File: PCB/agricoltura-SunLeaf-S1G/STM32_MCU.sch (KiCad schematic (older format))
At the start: 34 parts

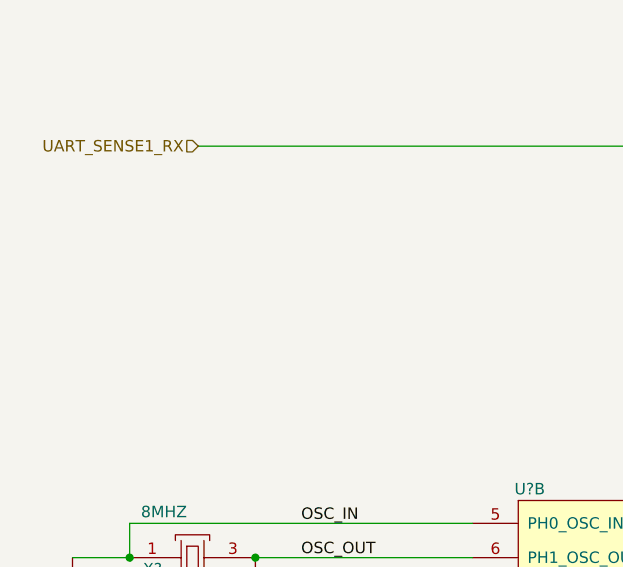
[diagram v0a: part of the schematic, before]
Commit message: Power Supply and Datasheets
Added datasheets for parts in use, designed power supply circuit
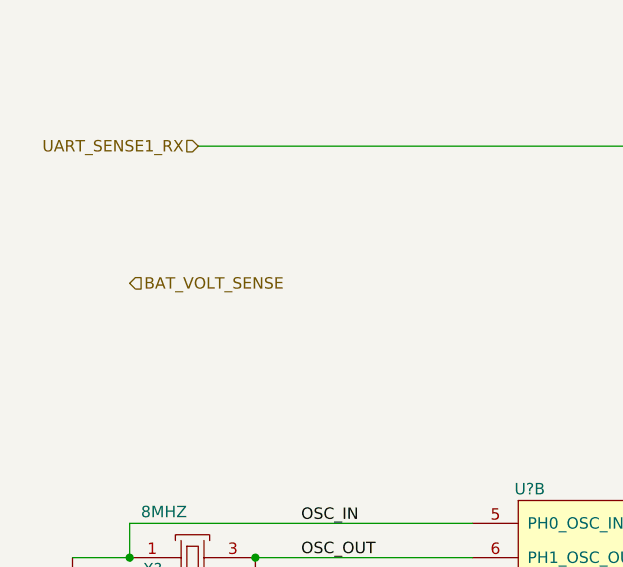
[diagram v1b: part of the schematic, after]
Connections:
- net labels added: BAT_VOLT_SENSE
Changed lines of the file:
@@
 Wire Wire Line
 	9200 2850 8100 2850
+Text HLabel 900  4350 2    50   Input ~ 0
+BAT_VOLT_SENSE
 $EndSCHEMATC

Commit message: Schematic Complete
Schematic completed and PCB started
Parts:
- added D1: LW_Q38G_Q1OO_3K6L_1, AVR-KiCAD-Lib-Diodes:LED0603, symbol AVR-KiCAD-Lib-Diodes:LW_Q38G_Q1OO_3K6L_1
- added L2: MI0603K300R-10, AVR-KiCAD-Lib-Inductors:MI0603K300R-10, symbol AVR-KiCAD-Lib-Inductors:MI0603K300R-10
- added R1: RC0402FR-071KL, AVR-KiCAD-Lib-Resistors:R0402, symbol AVR-KiCAD-Lib-Resistors:RC0402FR-071KL
- added R10: RC0402FR-0710KL, AVR-KiCAD-Lib-Resistors:R0402, symbol AVR-KiCAD-Lib-Resistors:RC0402FR-0710KL
- added R11, R12: RC0402FR-0722RL, AVR-KiCAD-Lib-Resistors:R0402, symbol AVR-KiCAD-Lib-Resistors:RC0402FR-0722RL
- added R14, R15, R18, R2, R3: RC0402FR-0733RL, AVR-KiCAD-Lib-Resistors:R0402, symbol AVR-KiCAD-Lib-Resistors:RC0402FR-0733RL
- gave numbers to parts that had none: 33
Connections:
- net labels added: BAT_VOLT_ADC123_IN10, CS_MCU, CS_RF, HEARBEAT_LED, I2C_SCL_MUX, I2C_SDA_MUX, MISO_MCU, MISO_RF, MOSI_MCU, MOSI_RF, RF_SHDN_MCU, SCLK_MCU, SCLK_RF, UART_MUX_E1, UART_MUX_EN, UART_MUX_S0, UART_TX, USB_VBUS_5V
- wire segments 124 -> 138
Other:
- note added: "STM32F446RET6 - ARM Cortex M4 MCU"
- moved on the sheet: C11, C12, C13, C14, L3, R17, R5, R6, R7, R8, R9, T2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

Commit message: PCB Progress
added TVS diodes fo QWIIC connector serial signals. Did more routing overall.
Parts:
- removed SW1: TL3301NF260QG, AVR-KiCAD-Lib-Mech-Switches:TL3301NF260QG, symbol AVR-KiCAD-Lib-Mech-Switches:TL3301NF260QG
- removed T1: BU2032SM-JJ-GTR, AVR-KiCAD-Lib-Battery-Holders:BU2032SM-JJ-GTR, symbol AVR-KiCAD-Lib-Battery-Holders:BU2032SM-JJ-GTR
- added H1, H2, H3, H4, H5, H6: M2_Plated_Hole, AVR-KiCAD-Lib-Holes_Fasteners:M2_HOLE, symbol AVR-KiCAD-Lib-Holes_Fasteners:M2_Plated_Hole
- added L4: BLM15HG601SN1D, AVR-KiCAD-Lib-Inductors:BLM15HG601SN1D, symbol AVR-KiCAD-Lib-Inductors:BLM15HG601SN1D
- added SW1: B3U-1000P, AVR-KiCAD-Lib-Mech-Switches:B3U-1000P, symbol AVR-KiCAD-Lib-Mech-Switches:B3U-1000P
- added T1: BM04B-SRSS-TB(LF)(SN), AVR-KiCAD-Lib-Connectors:CONN_BM04B-SRSS-TB(LF)(SN), symbol AVR-KiCAD-Lib-Connectors:BM04B-SRSS-TB(LF)(SN)
- added T18, T19: PPTC101LFBN-RC, AVR-KiCAD-Lib-Connectors:Female_Header_Straight_1x10_Pitch2.54mm, symbol AVR-KiCAD-Lib-Connectors:PPTC101LFBN-RC
- added T20: BU2032SM-JJ-GTR, AVR-KiCAD-Lib-Battery-Holders:BU2032SM-JJ-GTR, symbol AVR-KiCAD-Lib-Battery-Holders:BU2032SM-JJ-GTR
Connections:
- net labels added: DEBUG_UART_RX, DEBUG_UART_TX, FGND, UART_RX
- wire segments 138 -> 151
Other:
- moved on the sheet: C11, R18

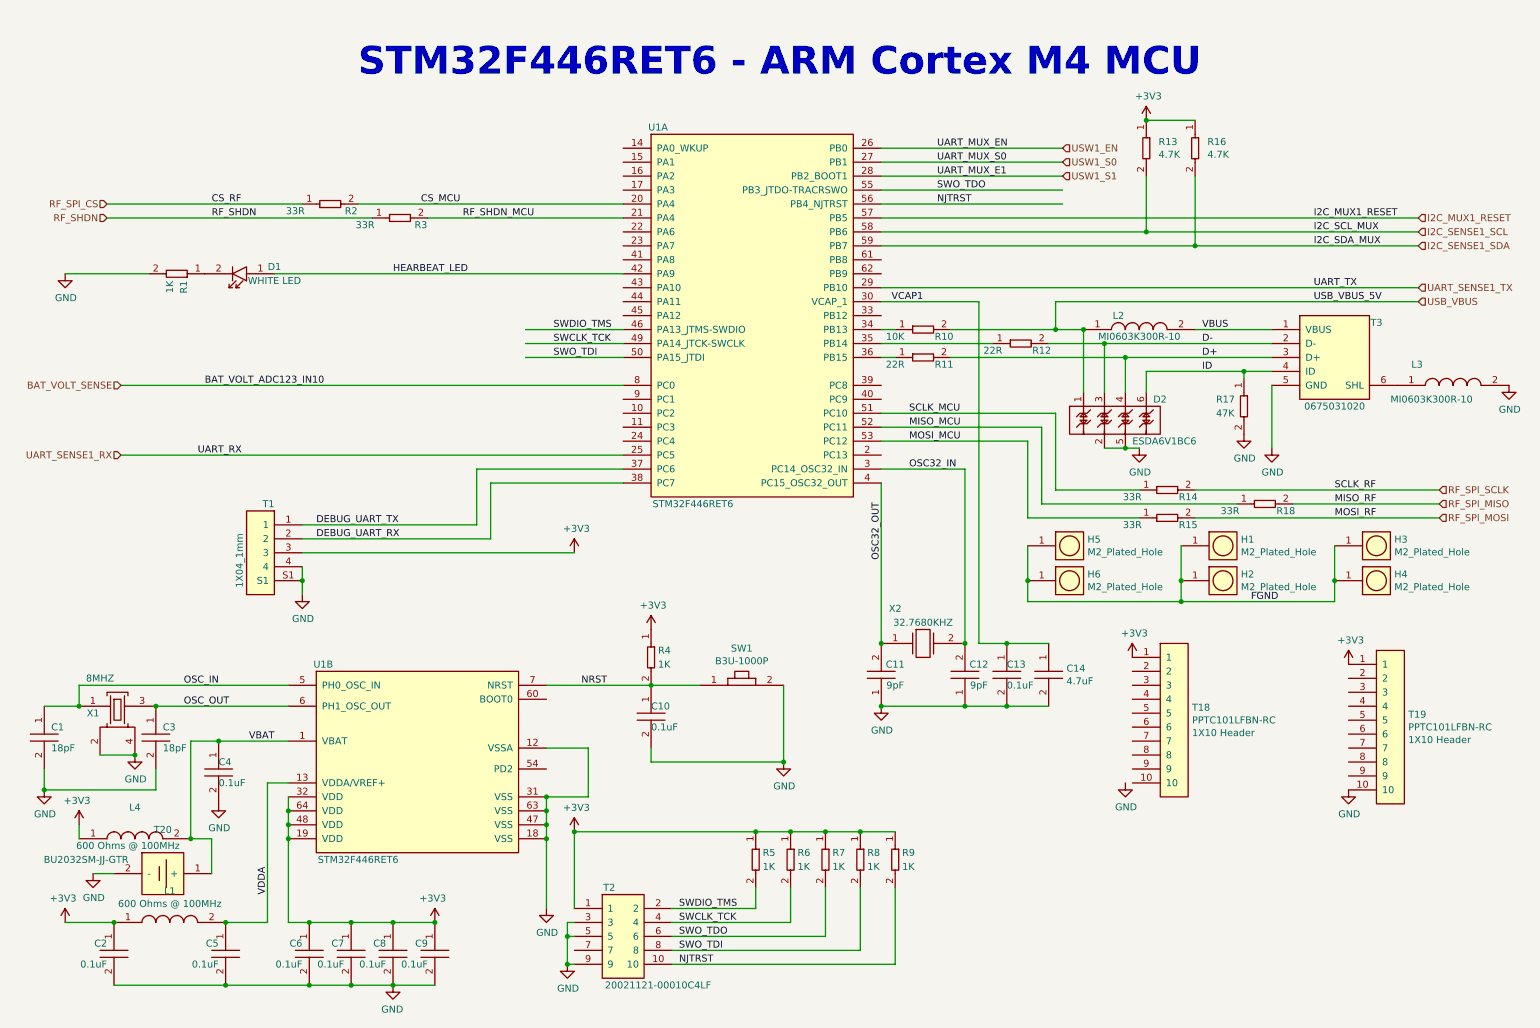
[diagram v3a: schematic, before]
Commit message: Pullups
Added pullup reistors to I2C ports, changed JTAG connector over to Tag connect.
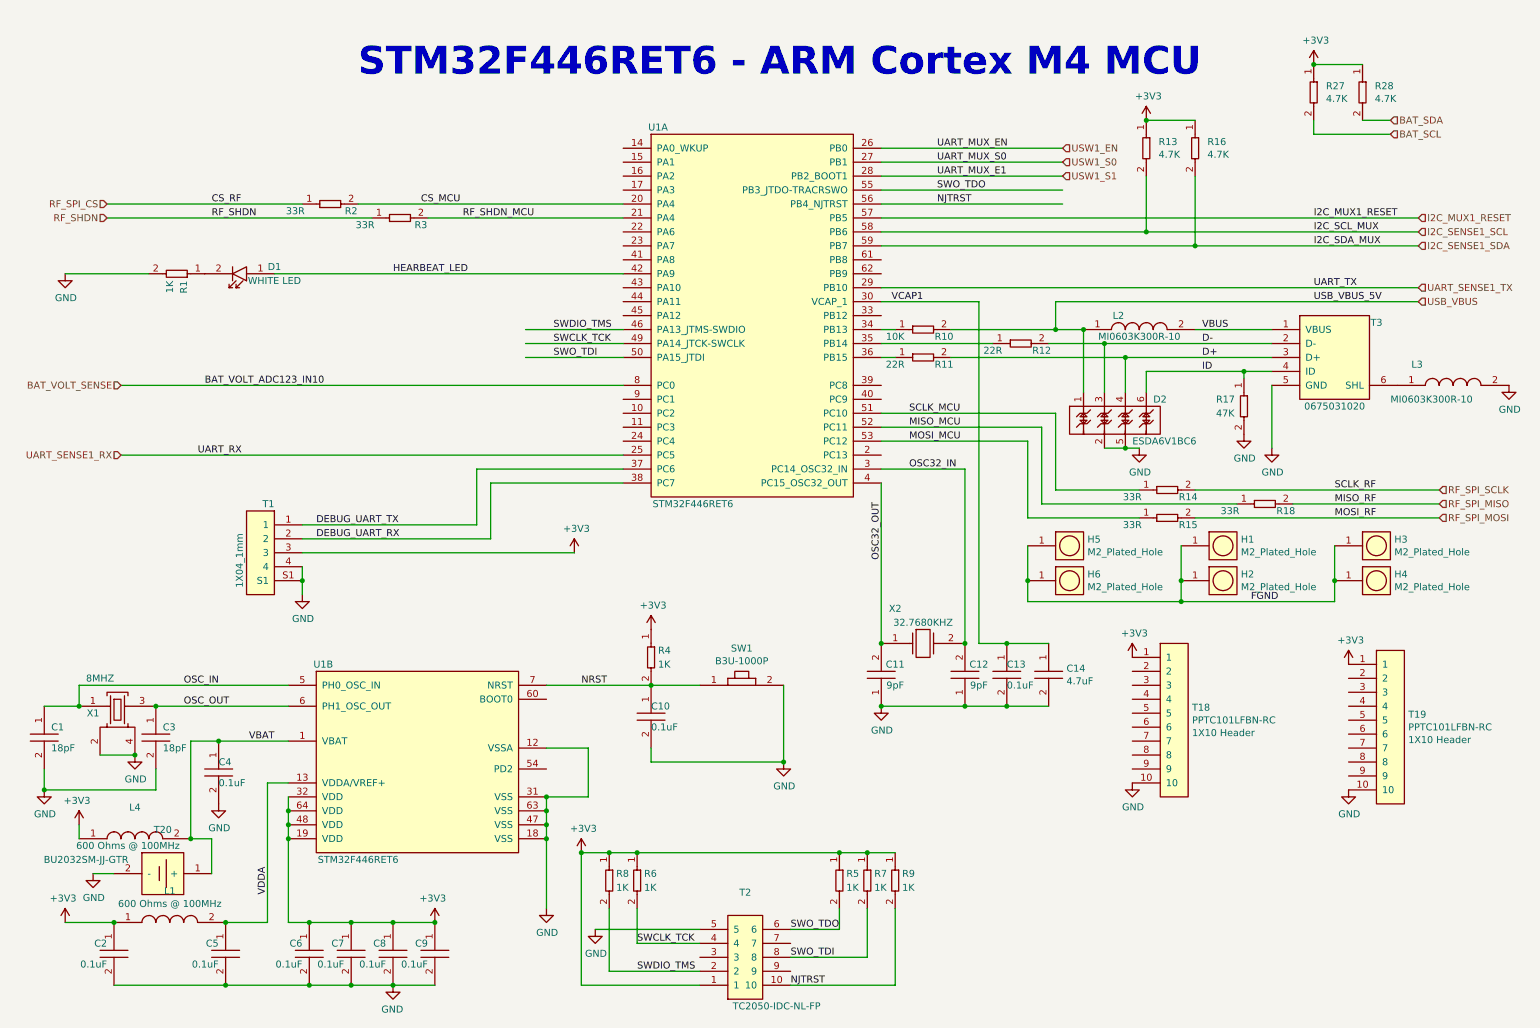
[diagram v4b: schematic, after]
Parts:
- removed T2: 20021121-00010C4LF, AVR-KiCAD-Lib-Connectors:20021121-00010C4LF, symbol AVR-KiCAD-Lib-Connectors:20021121-00010C4LF
- added R27, R28: RC0402FR-074K7L, AVR-KiCAD-Lib-Resistors:R0402, symbol AVR-KiCAD-Lib-Resistors:RC0402FR-074K7L
- added T2: TC2050-IDC-NL-FP, AVR-KiCAD-Lib-Connectors:TC2050-CLIP, symbol AVR-KiCAD-Lib-Connectors:TC2050-IDC-NL-FP
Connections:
- net labels added: BAT_SCL, BAT_SDA
- wire segments 151 -> 152
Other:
- moved on the sheet: R5, R6, R7, R8, R9

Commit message: PCB Progress
PCB routing progress made, USB port replaced with micro b like older sunleaf designs.
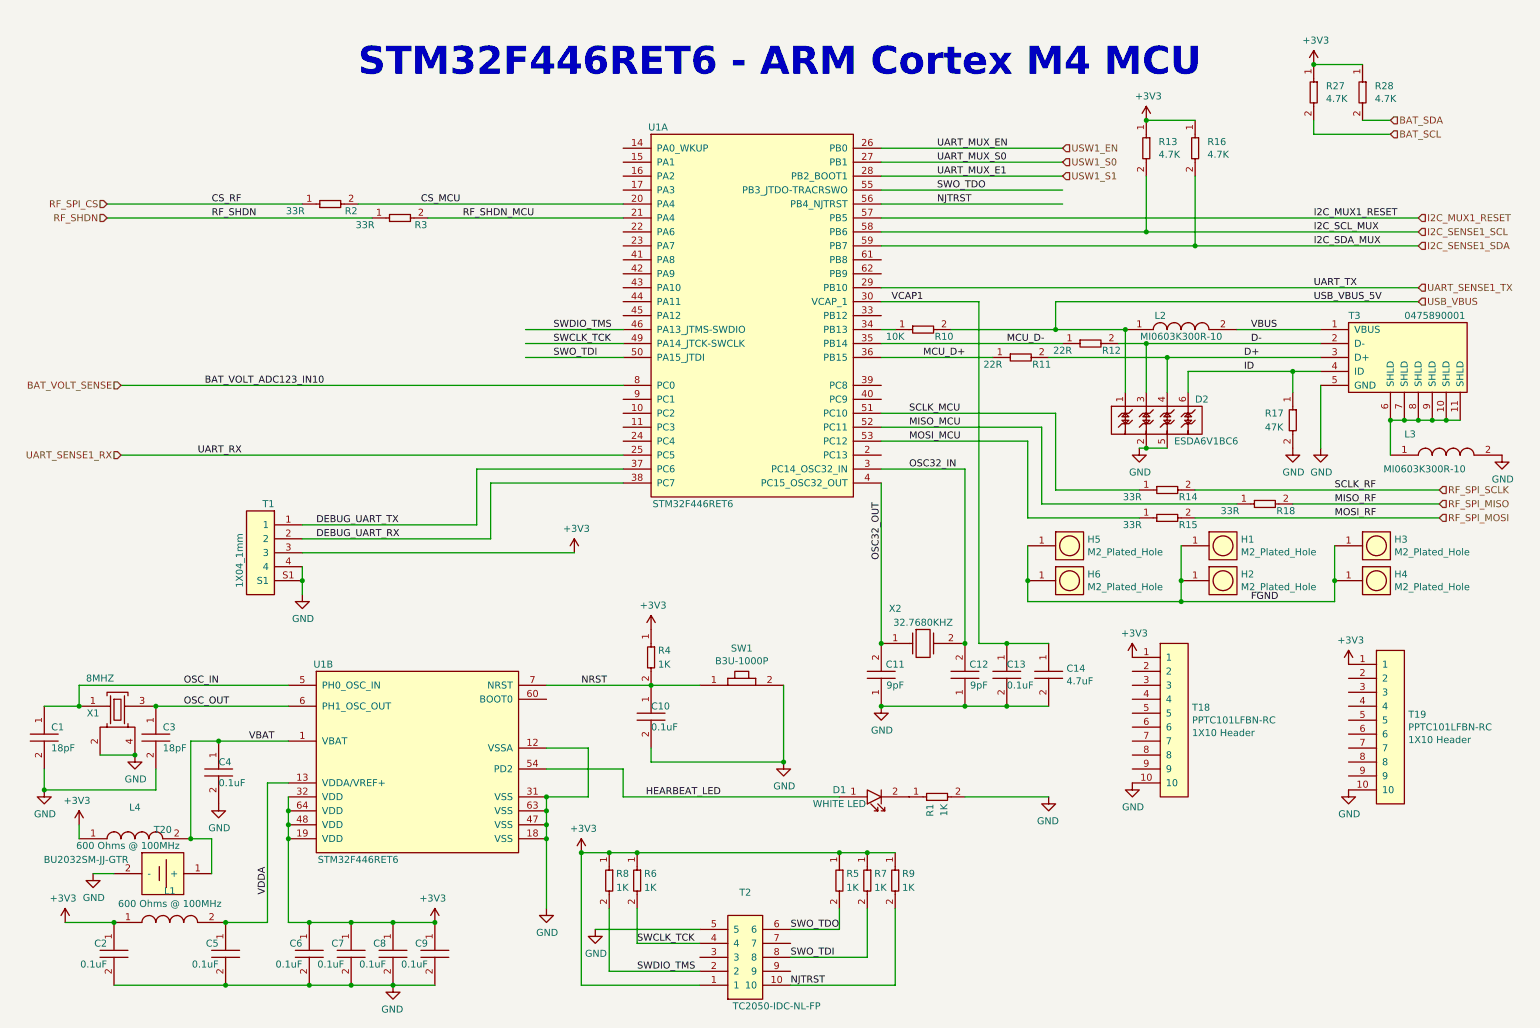
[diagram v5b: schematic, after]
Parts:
- removed T3: 0675031020, AVR-KiCAD-Lib-Connectors:USB_Mini-B, symbol AVR-KiCAD-Lib-Connectors:0675031020
- added T3: 0475890001, AVR-KiCAD-Lib-Connectors:0475890001, symbol AVR-KiCAD-Lib-Connectors:0475890001
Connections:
- net labels added: MCU_D+, MCU_D-
- wire segments 152 -> 160
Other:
- moved on the sheet: D1, D2, L2, L3, R1, R11, R12, R17

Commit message: Routing Complete
Board routing completed, also added EEPROM for storing configuration settings.
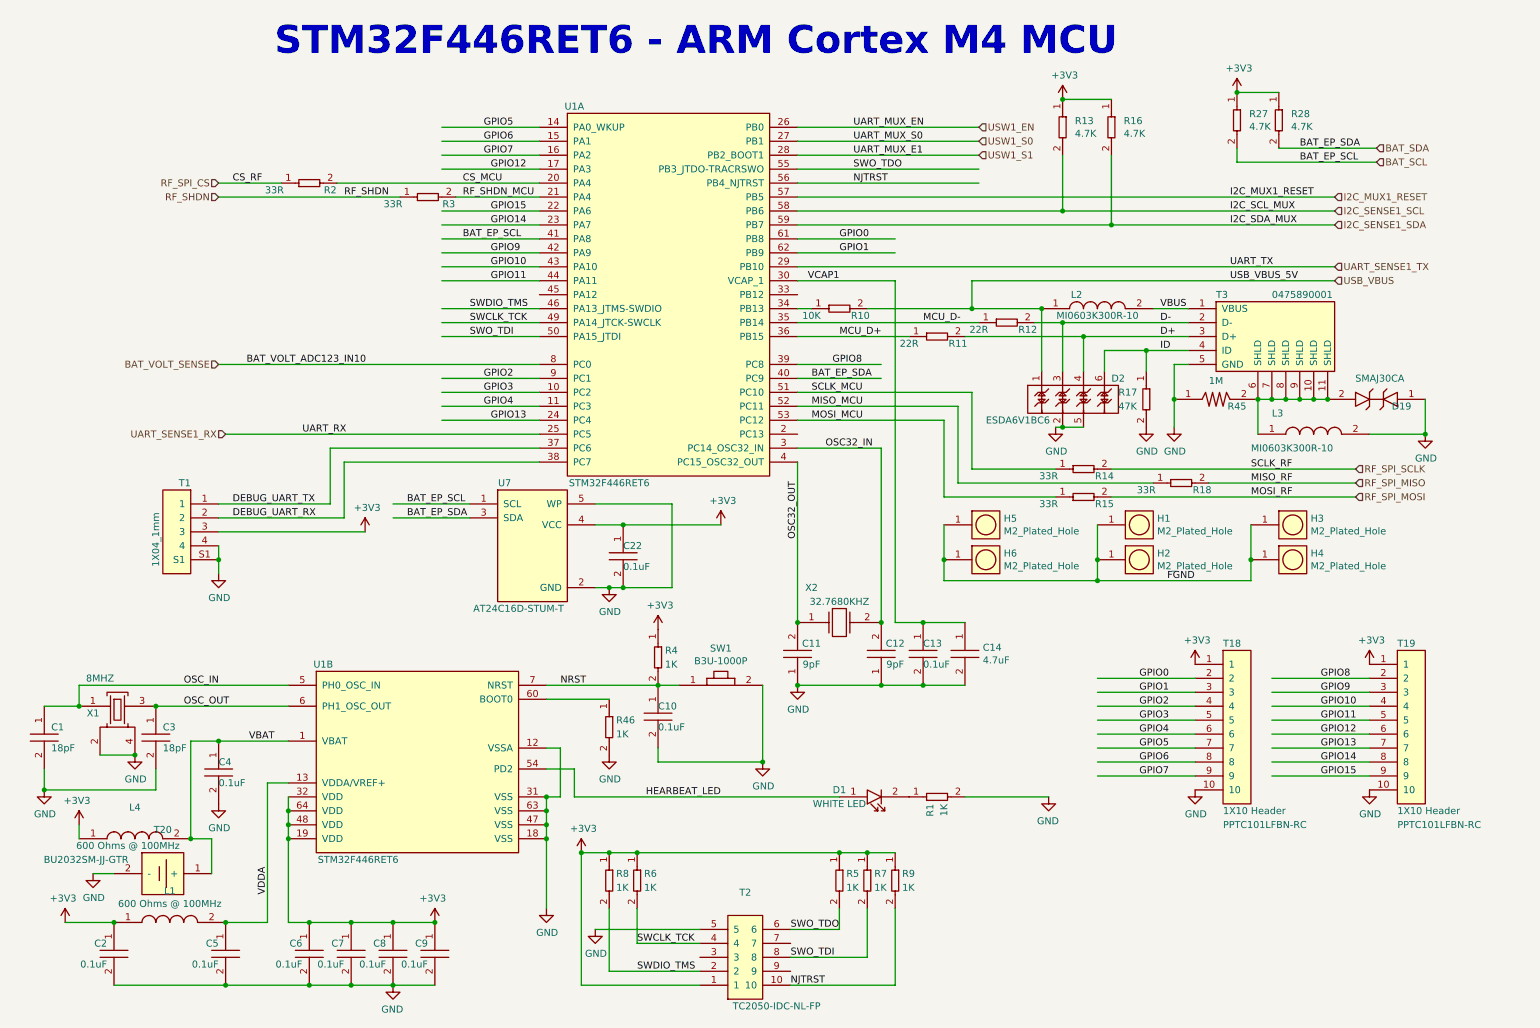
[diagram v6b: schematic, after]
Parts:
- added C22: C0402C104K9PACTU, AVR-KiCAD-Lib-Resistors:R0402, symbol AVR-KiCAD-Lib-Capacitors:C0402C104K9PACTU
- added D19: SMAJ30CA, AVR-KiCAD-Lib-Diodes:SMAJ30CA, symbol AVR-KiCAD-Lib-Diodes:SMAJ30CA
- added R45: RC1206FR-071ML, AVR-KiCAD-Lib-Resistors:R1206, symbol AVR-KiCAD-Lib-Resistors:RC1206FR-071ML
- added R46: RC0402FR-071KL, AVR-KiCAD-Lib-Resistors:R0402, symbol AVR-KiCAD-Lib-Resistors:RC0402FR-071KL
- added U7: AT24C16D-STUM-T, AVR-KiCAD-Lib-ICs:SOT-23-5, symbol AVR-KiCAD-Lib-ICs:AT24C16D-STUM-T
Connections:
- net labels added: BAT_EP_SCL, BAT_EP_SDA, GPIO0, GPIO1, GPIO10, GPIO11, GPIO12, GPIO13, GPIO14, GPIO15, GPIO2, GPIO3, GPIO4, GPIO5, GPIO6, GPIO7, GPIO8, GPIO9
- wire segments 160 -> 208
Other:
- moved on the sheet: C10, C11, C12, C13, C14, D2, H1, H2, H3, H4, H5, H6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
